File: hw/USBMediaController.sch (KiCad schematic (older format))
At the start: 34 parts, among them J1 CONN_01X03, J2 JTAG, J3 USB_B, J4 CONN_01X03, SW1 SKQGAKE010, SW2 SW_PUSH, SW3 SW_PUSH, SW4 SW_PUSH, SW5 SW_PUSH, SW6 R10307RN02Q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

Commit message: Schematic edits: fix BSL and USB pullup, and some footprints
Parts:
- removed J4: CONN_01X03, symbol CONN_01X03
- added C10, C11: ??, Capacitors_SMD:C_0603_HandSoldering, symbol C_Small
- added SW9: SKQGADE010, Local:sw-SKQGADE010, symbol SW_PUSH
- added Y1: 4mhz, symbol Crystal_Small
- C2, C3, C4, C5, C6, C7, C8, C9: footprint (none) -> Capacitors_SMD:C_0603_HandSoldering
- J1: footprint (none) -> Pin_Headers:Pin_Header_Straight_1x03
- J2: footprint (none) -> Socket_Strips:Socket_Strip_Straight_2x07
- J3: footprint (none) -> Connect:USB_B
- R1, R10, R11, R12, R2, R3, R4, R5, R8, R9: footprint (none) -> Resistors_SMD:R_0603_HandSoldering
- R6: value 35K -> 1.5K; footprint (none) -> Resistors_SMD:R_0603_HandSoldering
- R7: value 10K -> 35K; footprint (none) -> Resistors_SMD:R_0603_HandSoldering
- SW1: value SKQGAKE010 -> SKQGADE010; footprint (none) -> Local:sw-SKQGADE010
- SW2, SW3, SW4, SW5: value SW_PUSH -> Cherry MX1A-11NN; footprint (none) -> Local:cherrymx_withpins
- SW6: renamed from SW7; value SW_PUSH -> Cherry MX1A-11NN; footprint (none) -> Local:cherrymx_withpins
- U1: footprint (none) -> Housings_QFP:LQFP-48_7x7mm_Pitch0.5mm
- renumbered SW6 to SW7
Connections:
- net +3V3: no longer R6.~
- net GND: now also C10.2, C11.1; no longer R7.~
- net at J3.3 (D+), U1.38 (PU.0/DP): now also R6.~
- net at U1.39 (PUR): now also R6.~, SW9.1
- net at U1.8 (P5.4/XIN): now also C10.1, Y1.1
- net at U1.9 (P5.5/XOUT): now also C11.2, Y1.2
- net at R7.~: now also SW9.2
- no-connect marks 21 -> 19
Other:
- note added: "BSL"
- note added: "RESET"
- note removed: "BSL\n\nAPP"
- note removed: "MODE"
- moved on the sheet: C1, C2, C4

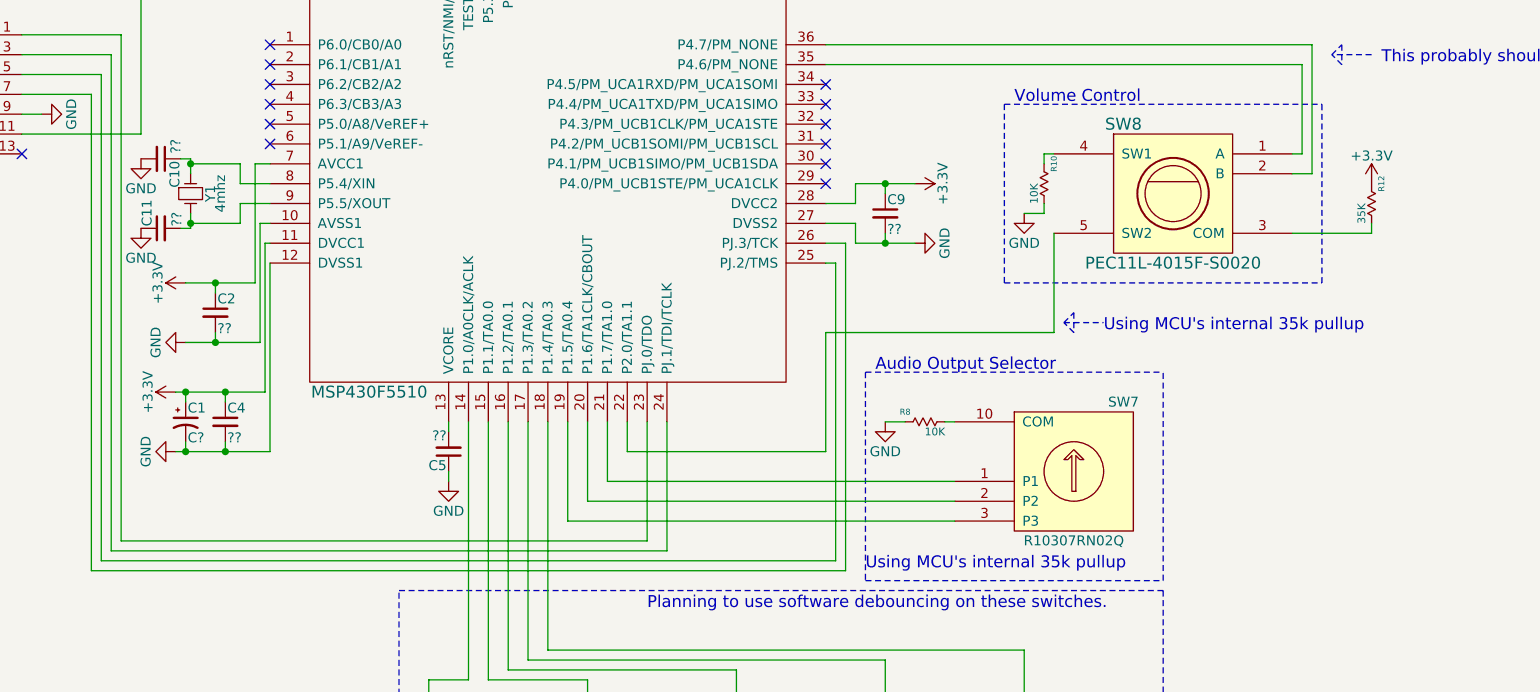
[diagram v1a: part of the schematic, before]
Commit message: More work on some USB and footprints
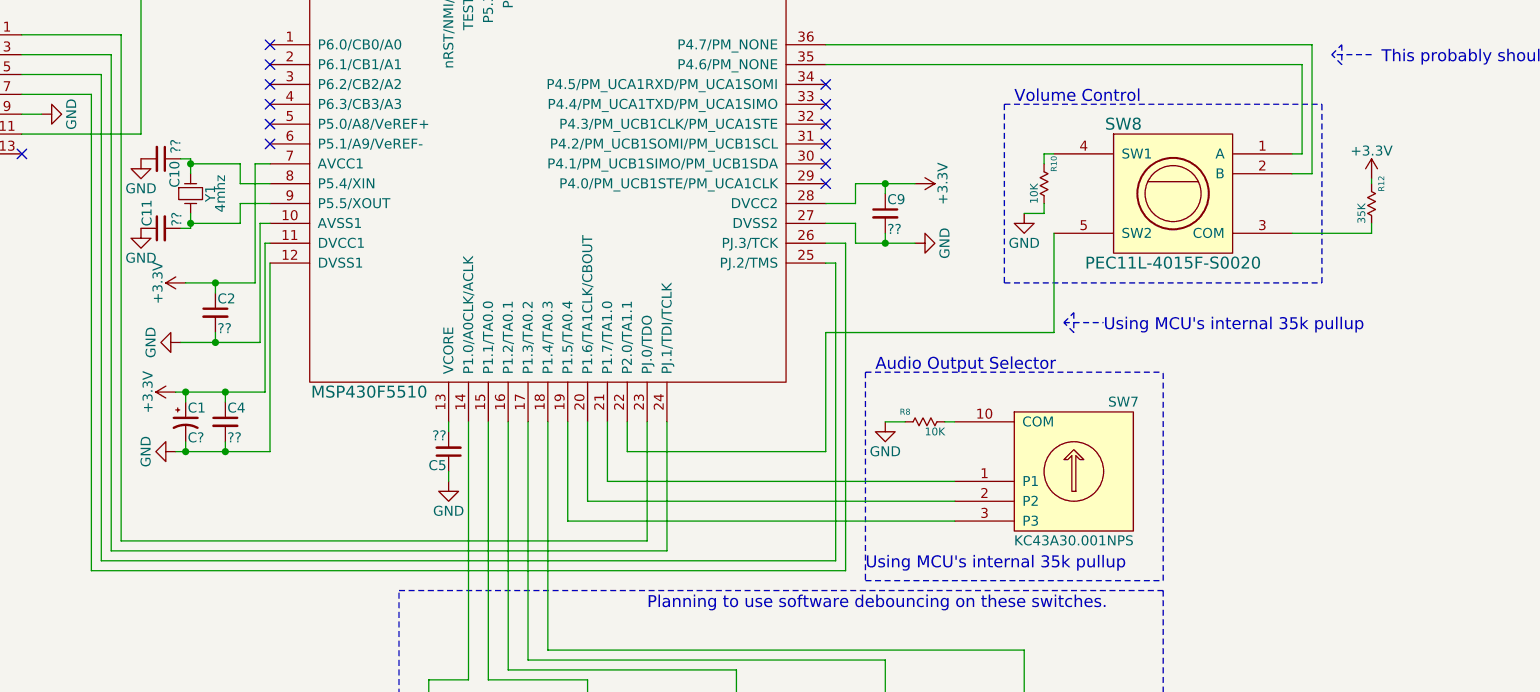
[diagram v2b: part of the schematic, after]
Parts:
- C1: footprint (none) -> Capacitors_SMD:c_elec_5x5.7
- SW7: value R10307RN02Q -> KC43A30.001NPS; footprint (none) -> Local:KC43A30.001NPS
- Y1: footprint (none) -> Crystals:Crystal_HC49-U_Vertical
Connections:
- net at R7.~: now also SW9.2
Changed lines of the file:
@@
 P 7050 4700
 F 0 "SW7" H 6800 5050 50  0000 C CNN
-F 1 "R10307RN02Q" H 7050 4351 50  0000 C CNN
-F 2 "" H 7050 4700 50  0001 C CNN
+F 1 "KC43A30.001NPS" H 7050 4351 50  0000 C CNN
+F 2 "Local:KC43A30.001NPS" H 7050 4700 50  0001 C CNN
 F 3 "" H 7050 4700 50  0000 C CNN
 	1    7050 4700
@@
 L GND #PWR011
 U 1 1 575F73E5
-P 2575 4050
-F 0 "#PWR011" H 2575 3800 50  0001 C CNN
-F 1 "GND" H 2575 3900 50  0000 C CNN
-F 2 "" H 2575 4050 50  0000 C CNN
-F 3 "" H 2575 4050 50  0000 C CNN
-	1    2575 4050
+P 2550 4050
+F 0 "#PWR011" H 2550 3800 50  0001 C CNN
+F 1 "GND" H 2550 3900 50  0000 C CNN
+F 2 "" H 2550 4050 50  0000 C CNN
+F 3 "" H 2550 4050 50  0000 C CNN
+	1    2550 4050
 	0    1    1    0
 $EndComp
@@
 L +3.3V #PWR023
 U 1 1 5760BFAC
-P 8550 3250
-F 0 "#PWR023" H 8550 3100 50  0001 C CNN
-F 1 "+3.3V" H 8550 3390 50  0000 C CNN
-F 2 "" H 8550 3250 50  0000 C CNN
-F 3 "" H 8550 3250 50  0000 C CNN
-	1    8550 3250
+P 8550 3225
+F 0 "#PWR023" H 8550 3075 50  0001 C CNN
+F 1 "+3.3V" H 8550 3365 50  0000 C CNN
+F 2 "" H 8550 3225 50  0000 C CNN
+F 3 "" H 8550 3225 50  0000 C CNN
+	1    8550 3225
 	1    0    0    -1
 $EndComp
@@
 F 0 "C1" H 2585 4520 50  0000 L CNN
 F 1 "C?" H 2585 4370 50  0000 L CNN
-F 2 "" H 2575 4450 50  0001 C CNN
+F 2 "Capacitors_SMD:c_elec_5x5.7" H 2575 4450 50  0001 C CNN
 F 3 "" H 2575 4450 50  0000 C CNN
 	1    2575 4450
@@
 	2725 4000 2725 4050
 Wire Wire Line
-	2575 4050 2950 4050
+	2550 4050 2950 4050
 Connection ~ 2725 4050
 Wire Wire Line
@@
 F 0 "Y1" H 2600 3400 50  0000 C CNN
 F 1 "4mhz" H 2600 3450 50  0000 C CNN
-F 2 "" H 2600 3300 50  0001 C CNN
+F 2 "Crystals:Crystal_HC49-U_Vertical" H 2600 3300 50  0001 C CNN
 F 3 "" H 2600 3300 50  0000 C CNN
 	1    2600 3300
@@
 	1    0    0    -1
 $EndComp
+Wire Wire Line
+	8550 3225 8550 3250
 $EndSCHEMATC
